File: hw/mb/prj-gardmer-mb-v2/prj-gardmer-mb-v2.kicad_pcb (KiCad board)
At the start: 2 copper layers, 147 x 71 mm, 176 parts, among them J1 Conn_01x05, J2 230VAC_IN, J3 Conn_01x04, J4 5VDC_IN, K1 AZ9371T-1A-5D, K2 AZ9371T-1A-5D, K3 AZ9371T-1A-5D, K4 AZ9371T-1A-5D, Q1 BC817, Q13 BC817, Q14 BC817, Q2 BC817, Q3 BC817, Q4 BC817, Q5 BC807, Q6 BC807, Q7 BC807, Q8 BC807, Q9 BC817, SW1 Reset_SW, SW10 Unlock_SW, SW2 Clear_SW, SW3 Minutes_SW, SW4 Hours_SW, SW5 Mode_SW, SW6 Relay1_SW, SW7 Relay2_SW, SW8 Relay3_SW, SW9 Relay4_SW, U1 PIC18F25Q10, U2 PCF8523T, U3 74LS166, U4 74HC595, U5 74HC595, U6 ULN2803A, U7 KW4-804AVB, U8 74HC595, Y1 8MHz, Y2 32.768kHz

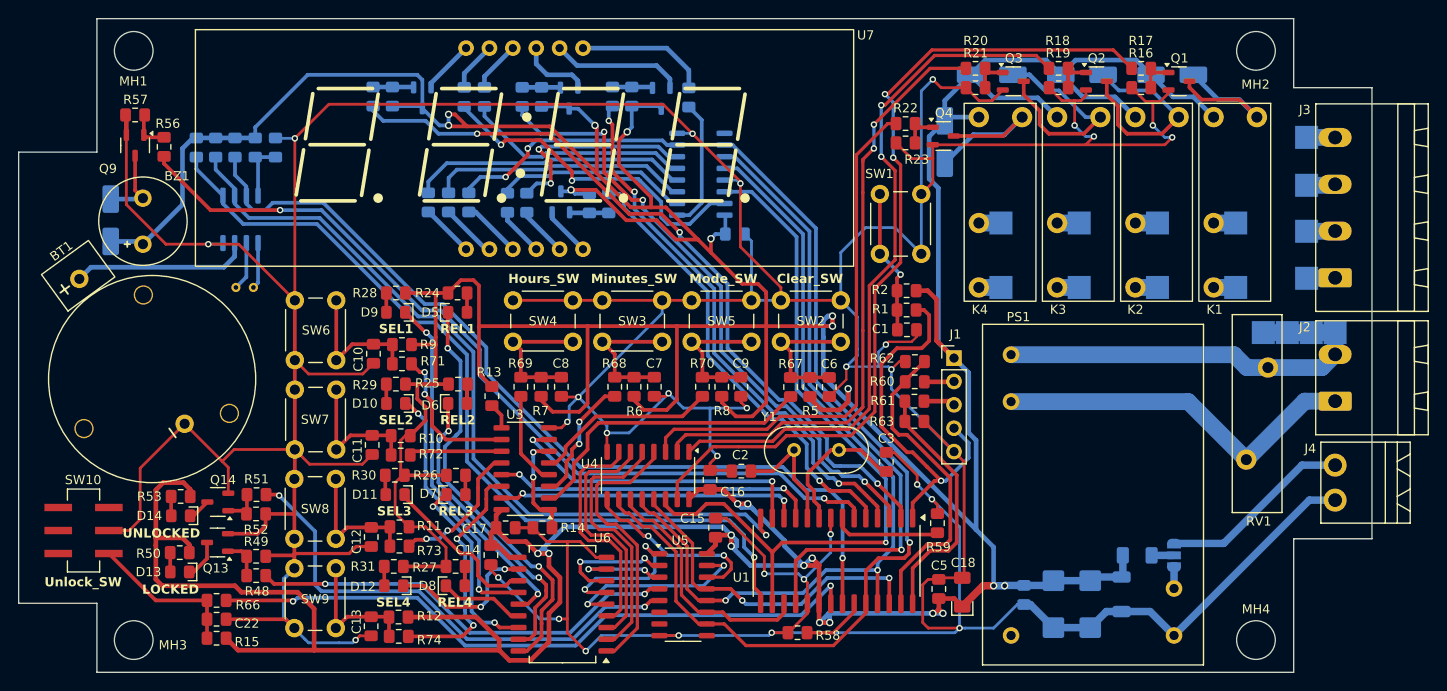
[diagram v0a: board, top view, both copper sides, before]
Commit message: Updated PCB: - improved 5V vias (they are now bigger and their pairs are connected on both layers in a prettier manner)
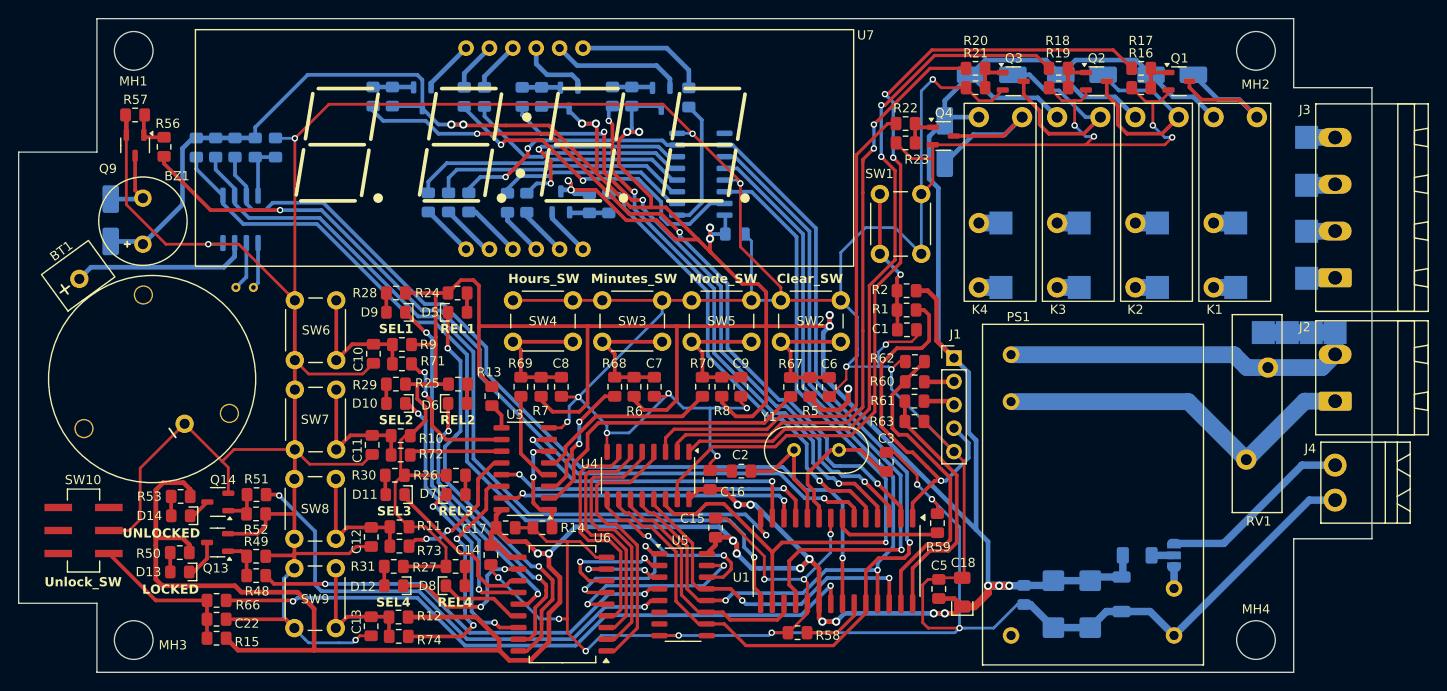
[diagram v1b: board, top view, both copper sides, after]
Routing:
- net +5V: track 709.0 -> 714.4 mm, vias 23 -> 28
- net /Display/S_SRCLK2_IN: track 68.0 -> 69.0 mm
- net Net-(U8-QA): track 36.7 -> 36.2 mm

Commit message: Updated PCB: - GND polygons poured - optimized tracks routing
Updated footprints:
- crc2032 holder mounting holes/pads has now copper removed
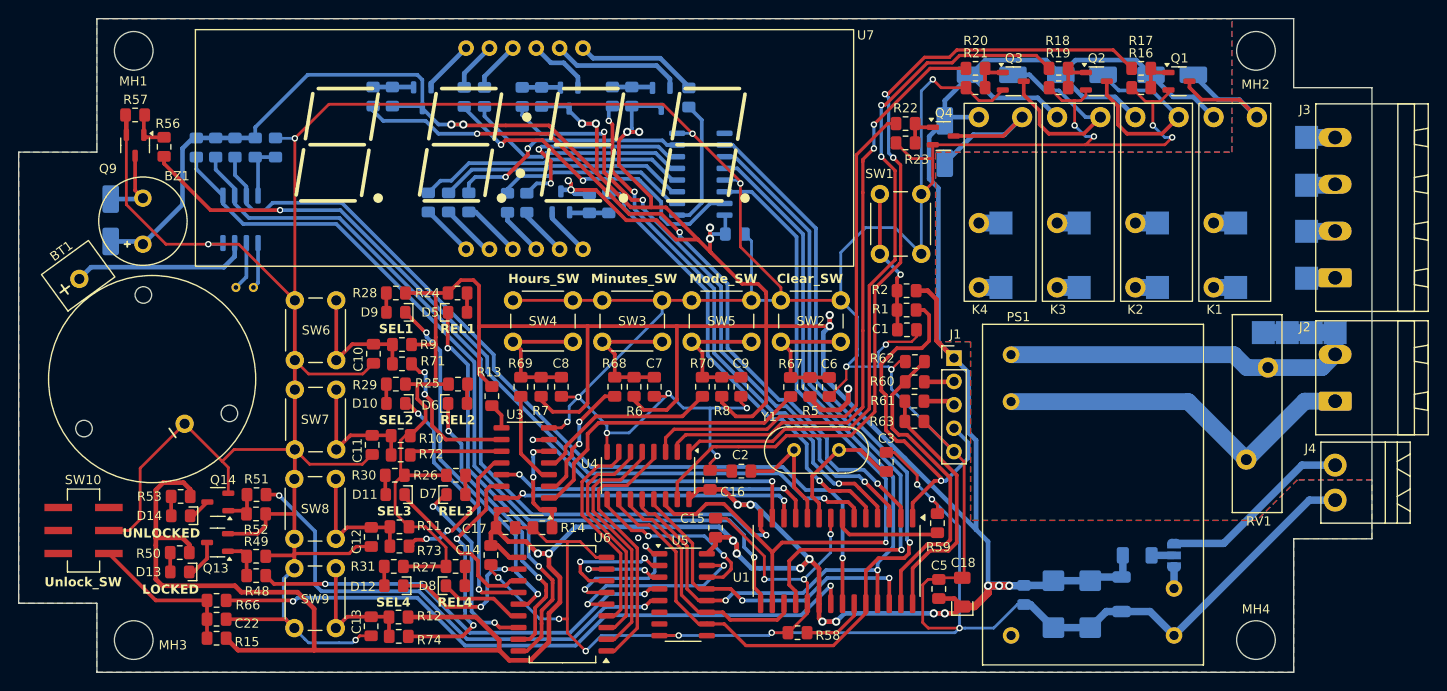
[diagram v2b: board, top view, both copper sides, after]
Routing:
- net /RelaysLeds/RELAY_LED4_EN: track 24.7 -> 22.5 mm
- net /RelaysLeds/RELAY_LED3_EN: track 27.4 -> 25.2 mm
- net /RelaysLeds/RELAY_LED2_EN: track 29.0 -> 27.2 mm
- net Net-(D5-K): track 45.5 -> 43.8 mm
- net Net-(D6-K): track 33.3 -> 32.1 mm
- net /RelaysLeds/RELAY_LED1_EN: track 30.4 -> 29.3 mm
- net Net-(U7-b): track 14.4 -> 13.4 mm
- net Net-(U8-QD): track 28.2 -> 27.2 mm
- net Net-(U1-RA7/OSC1): track 15.9 -> 15.1 mm
- net Net-(Q6-E): track 7.76 -> 6.98 mm
- net Net-(U8-QE): track 30.2 -> 29.5 mm
- net Net-(U1-INT1/RB1): track 97.1 -> 96.4 mm
- net Net-(U1-RA4): track 94.0 -> 93.3 mm
- net GND: vias 30 -> 31
- added copper zone on B.Cu, net GND
- added copper zone on F.Cu, net GND

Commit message: Updated PCB: - GND polygons optimized by adding essential vias and improving routing of few tracks
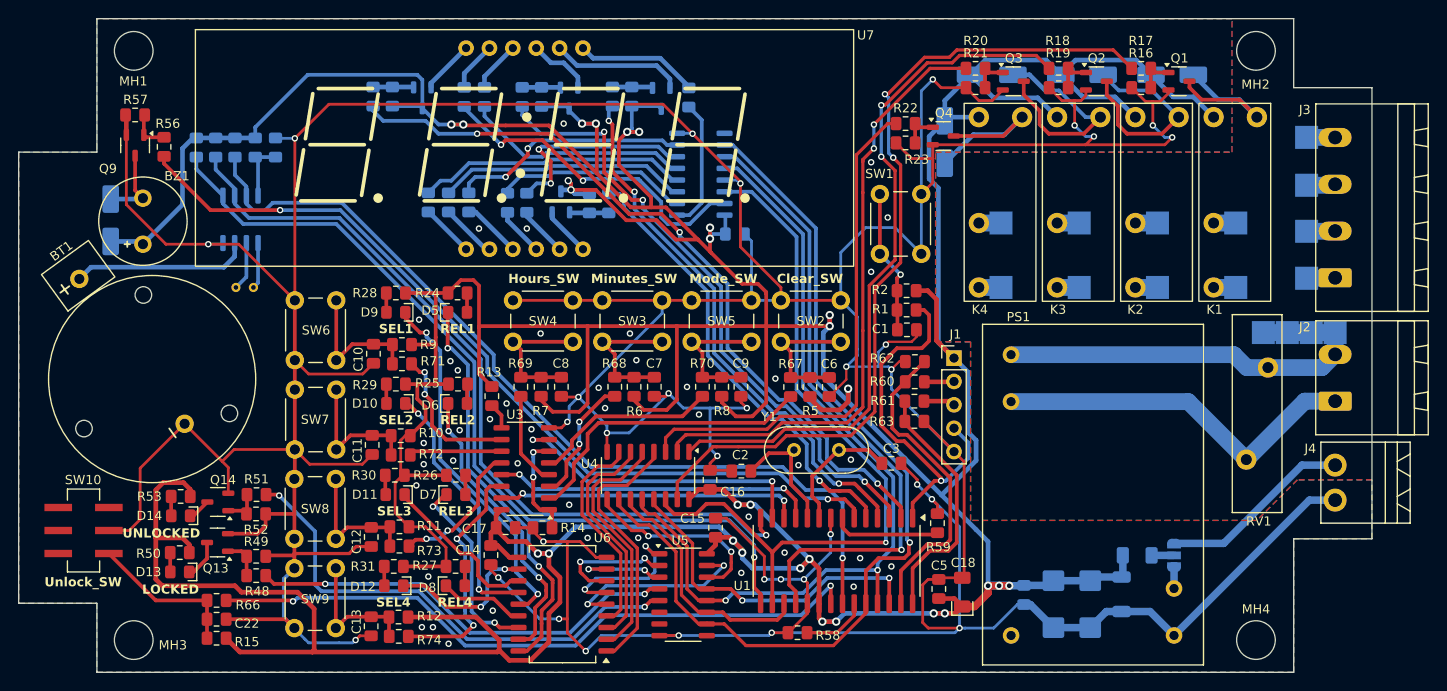
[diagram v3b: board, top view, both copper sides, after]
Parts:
- moved C3 0.57 mm to (169.8, 103.6), turned to 180 degrees
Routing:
- net GND: track 714.8 -> 712.7 mm, vias 31 -> 74
- net +5V: track 714.4 -> 712.7 mm
- net Net-(U1-RA7/OSC1): track 15.1 -> 14.2 mm
- net Net-(U4-QH'): track 20.5 -> 21.2 mm

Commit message: Updated PCB: - filled GND planes with vias - added board name and revision on the silkscreen layer, at the bottom right corner of the board
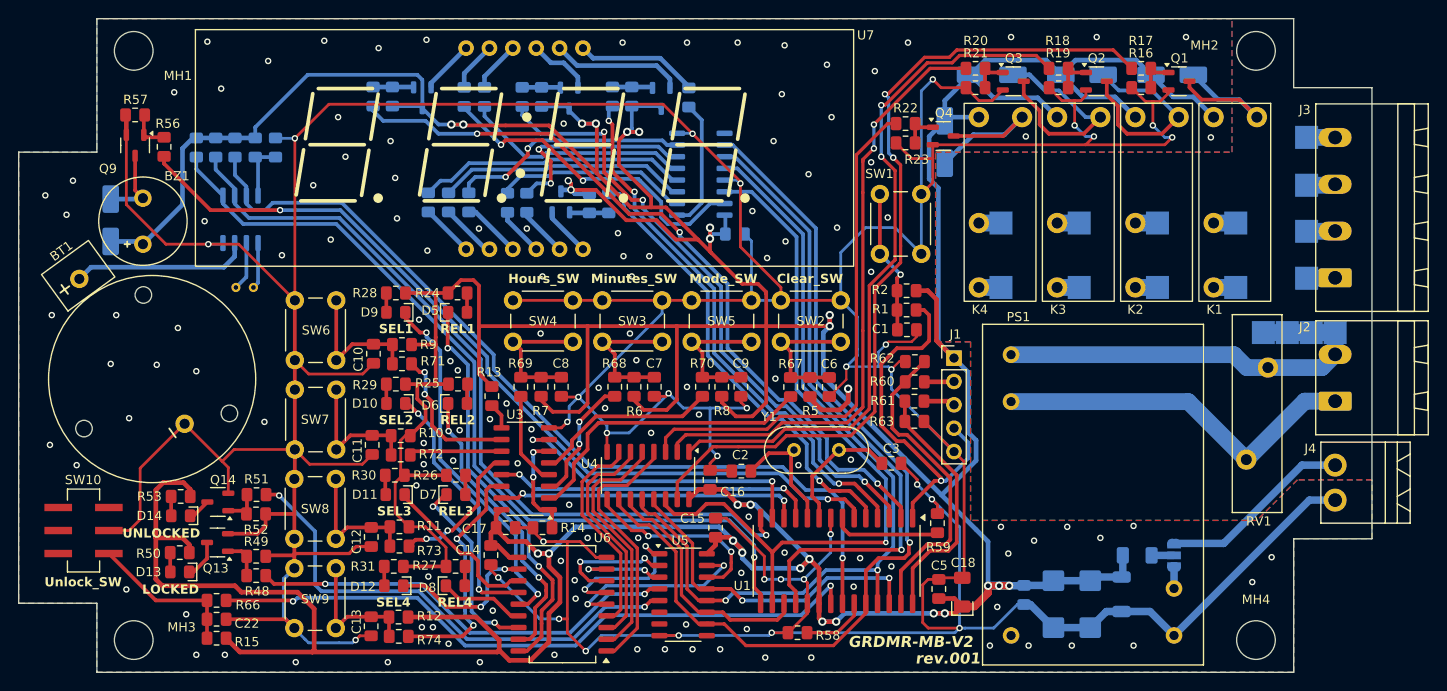
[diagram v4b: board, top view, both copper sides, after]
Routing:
- net GND: vias 74 -> 162
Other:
- board text added: "GRDMR-MB-V2"
- board text added: "rev.001"
